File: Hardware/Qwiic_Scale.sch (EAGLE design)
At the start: 32 parts, among them J1 JUMPER-SMT_2_NC_TRACE_SILK, J2 Qwiic Right Angle, J3 PTH, J4 Qwiic Right Angle, J6 Spring Terminal, U1 NAU7802

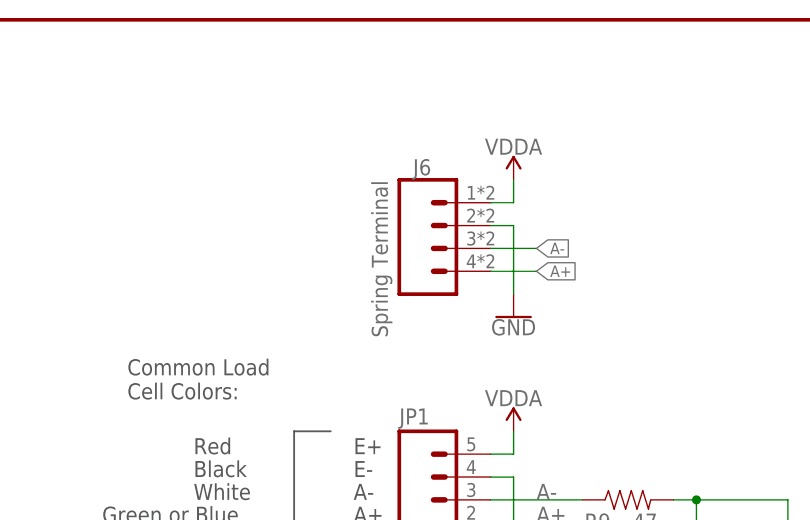
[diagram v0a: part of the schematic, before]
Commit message: Fixing FP on terminal. Adding ignore.
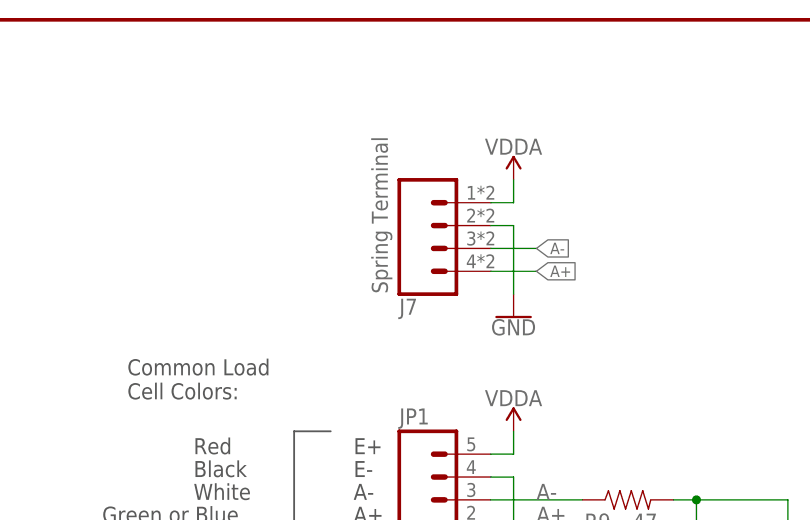
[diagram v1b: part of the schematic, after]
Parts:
- renumbered J6 to J7
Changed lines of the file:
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@@
 <part name="GND1" library="SparkFun-PowerSymbols" deviceset="GND" device=""/>
 <part name="U$10" library="SparkFun-PowerSymbols" deviceset="VDDA" device=""/>
-<part name="J6" library="SparkFun-Connectors" deviceset="CONN_04" device="SPRING" value="Spring Terminal"/>
 <part name="JP3" library="SparkFun-Jumpers" deviceset="JUMPER-SMT_3_2-NC_TRACE" device="_SILK" value="I2C"/>
 <part name="SUPPLY1" library="SparkFun-PowerSymbols" deviceset="3.3V" device=""/>
 <part name="R2" library="SparkFun-Resistors" deviceset="2.2KOHM" device="-0603-1/10W-1%" value="2.2k"/>
 <part name="R3" library="SparkFun-Resistors" deviceset="2.2KOHM" device="-0603-1/10W-1%" value="2.2k"/>
+<part name="J7" library="SparkFun-Connectors" deviceset="CONN_04" device="SPRING" value="Spring Terminal"/>
 </parts>
 <sheets>
@@
 <attribute name="VALUE" x="83.82" y="170.434" size="1.778" layer="96" font="vector" align="bottom-center"/>
 </instance>
-<instance part="J6" gate="J1" x="76.2" y="162.56" smashed="yes" rot="MR180">
-<attribute name="VALUE" x="69.85" y="150.114" size="1.778" layer="96" font="vector" rot="R90"/>
-<attribute name="NAME" x="72.644" y="168.148" size="1.778" layer="95" font="vector"/>
-</instance>
 <instance part="JP3" gate="G$1" x="180.34" y="134.62" smashed="yes" rot="R270">
 <attribute name="NAME" x="181.356" y="136.652" size="1.778" layer="95" font="vector"/>
@@
 <attribute name="NAME" x="186.436" y="127" size="1.778" layer="95" font="vector" rot="R90" align="bottom-center"/>
 <attribute name="VALUE" x="189.484" y="127" size="1.778" layer="96" font="vector" rot="R90" align="top-center"/>
+</instance>
+<instance part="J7" gate="J1" x="76.2" y="162.56" smashed="yes" rot="MR180">
+<attribute name="VALUE" x="69.85" y="172.466" size="1.778" layer="96" font="vector" rot="MR270"/>
+<attribute name="NAME" x="71.12" y="154.432" size="1.778" layer="95" font="vector" rot="MR180"/>
 </instance>
 </instances>
@@
 <wire x1="83.82" y1="162.56" x2="83.82" y2="154.94" width="0.1524" layer="91"/>
 <pinref part="GND1" gate="1" pin="GND"/>
-<pinref part="J6" gate="J1" pin="2"/>
+<pinref part="J7" gate="J1" pin="2"/>
 </segment>
 </net>
@@
 <wire x1="83.82" y1="165.1" x2="83.82" y2="167.64" width="0.1524" layer="91"/>
 <pinref part="U$10" gate="G$1" pin="VDDA"/>
-<pinref part="J6" gate="J1" pin="1"/>
+<pinref part="J7" gate="J1" pin="1"/>
 </segment>
 </net>
@@
 <wire x1="81.28" y1="160.02" x2="86.36" y2="160.02" width="0.1524" layer="91"/>
 <label x="86.36" y="160.02" size="1.27" layer="95" font="vector" xref="yes"/>
-<pinref part="J6" gate="J1" pin="3"/>
+<pinref part="J7" gate="J1" pin="3"/>
 </segment>
 </net>
@@
 <wire x1="81.28" y1="157.48" x2="86.36" y2="157.48" width="0.1524" layer="91"/>
 <label x="86.36" y="157.48" size="1.27" layer="95" font="vector" xref="yes"/>
-<pinref part="J6" gate="J1" pin="4"/>
-</segment>
-</net>
+<pinref part="J7" gate="J1" pin="4"/>
+</segment>
+</net>
